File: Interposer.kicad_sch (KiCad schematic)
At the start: 22 parts, among them J19 Conn_01x04_Pin, U13 TCA9548APWR, U14 ESP32-DEVKIT-V1

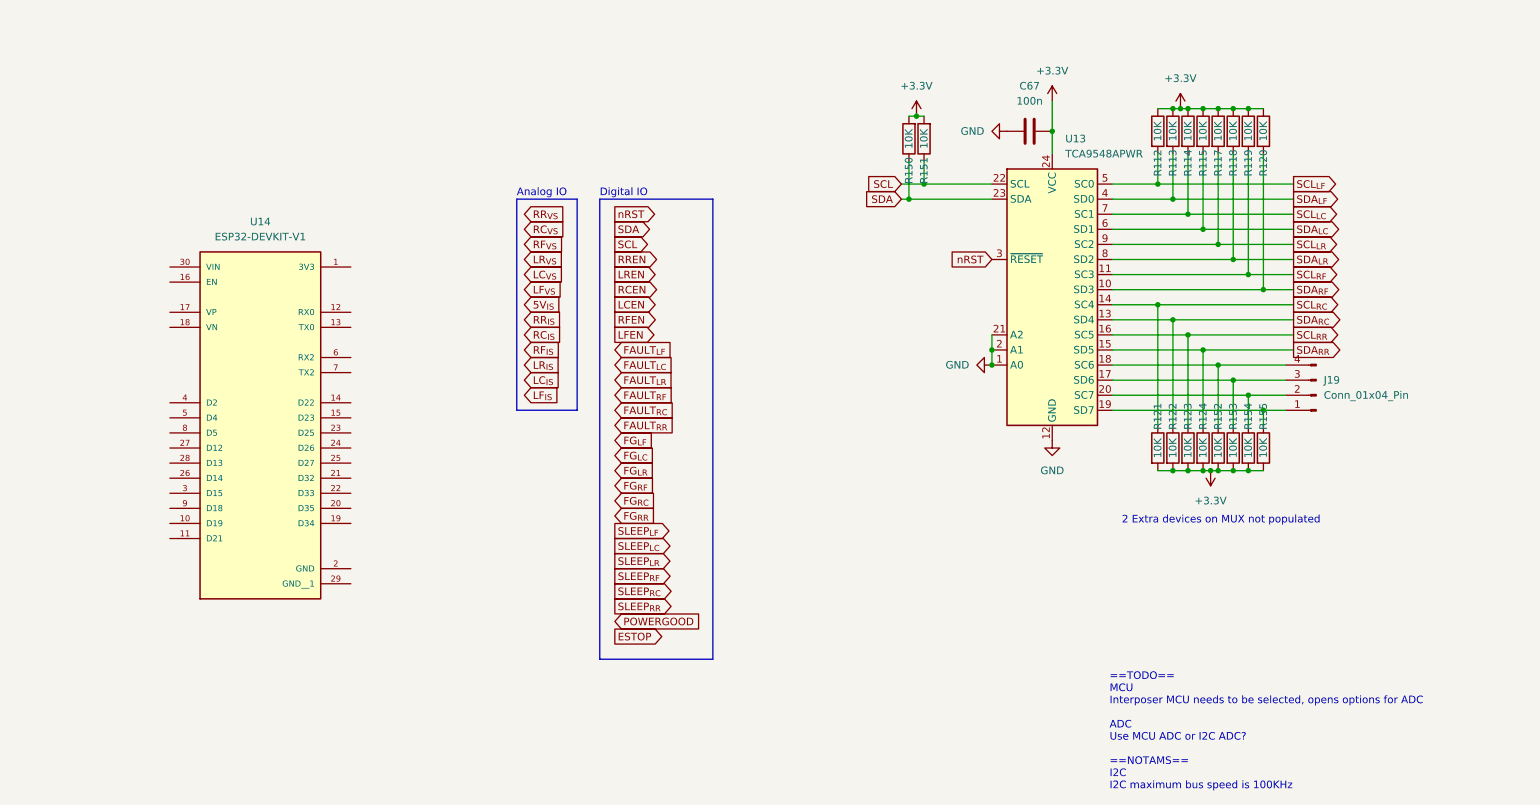
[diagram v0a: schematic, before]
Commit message: The great decluttering
Moved all possible controls to I2C, part selection commenced, IOs assigned pending comms schema
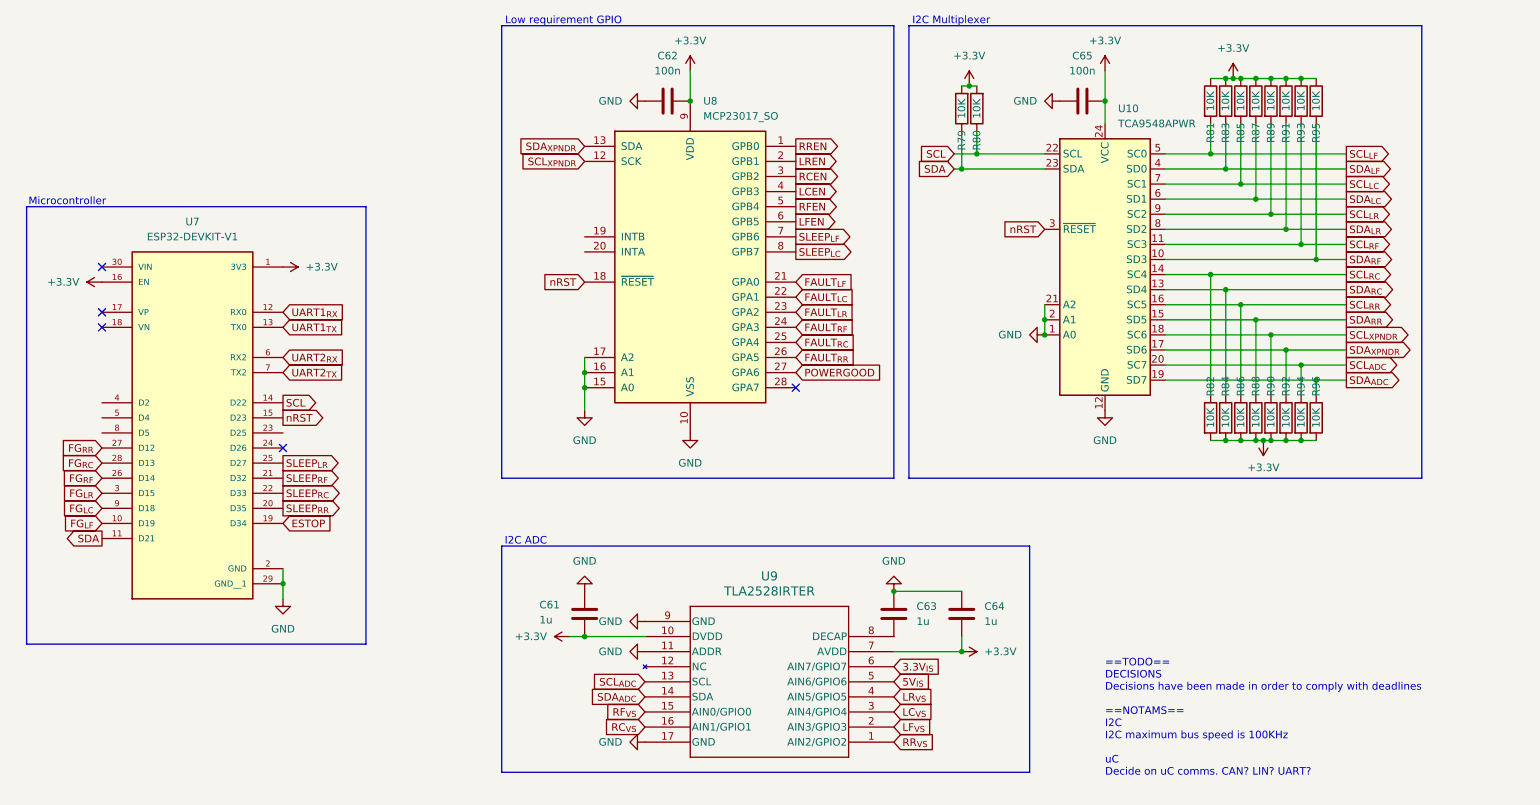
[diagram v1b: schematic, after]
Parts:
- removed J19: Conn_01x04_Pin, symbol Connector:Conn_01x04_Pin
- added C61, C63, C64: 1u, Capacitor_SMD:C_0603_1608Metric, symbol Device:C
- added C62: 100n, Capacitor_SMD:C_0603_1608Metric, symbol Device:C
- added U8: MCP23017_SO, Package_SO:SOIC-28W_7.5x17.9mm_P1.27mm, symbol Interface_Expansion:MCP23017_SO
- added U9: TLA2528IRTER, WQFN16_RTE_TEX, symbol TLA2528IRTER:TLA2528IRTER
- renumbered C67 to C65, R150 to R79, R151 to R80, R112 to R81, R121 to R82, R113 to R83, R122 to R84, R114 to R85, R123 to R86, R115 to R87, R124 to R88, R117 to R89, R152 to R90, R118 to R91, R153 to R92, R119 to R93, R154 to R94, R120 to R95, R155 to R96, U13 to U10, U14 to U7
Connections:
- net +3.3V: now also U7.1 (3V3), U7.16 (EN), C61.1, C62.2, C64.2, U8.9 (VDD), U9.10 (DVDD), U9.7 (AVDD)
- net 5V_{IS}: now also U9.5 (AIN6/GPIO6)
- net ESTOP: now also U7.19 (D34)
- net FAULT_{LC}: now also U8.22 (GPA1)
- net FAULT_{LF}: now also U8.21 (GPA0)
- net FAULT_{LR}: now also U8.23 (GPA2)
- net FAULT_{RC}: now also U8.25 (GPA4)
- net FAULT_{RF}: now also U8.24 (GPA3)
- net FAULT_{RR}: now also U8.26 (GPA5)
- net FG_{LC}: now also U7.9 (D18)
- net FG_{LF}: now also U7.10 (D19)
- net FG_{LR}: now also U7.3 (D15)
- net FG_{RC}: now also U7.28 (D13)
- net FG_{RF}: now also U7.26 (D14)
- net FG_{RR}: now also U7.27 (D12)
- net GND: now also U7.2 (GND), U7.29 (GND__1), C61.2, C62.1, C63.1, C64.1, U8.10 (VSS), U8.15 (A0), U8.16 (A1), U8.17 (A2), U9.11 (ADDR), U9.17 (GND), U9.9 (GND)
- net LCEN: now also U8.4 (GPB3)
- net LC_{VS}: now also U9.3 (AIN4/GPIO4)
- net LFEN: now also U8.6 (GPB5)
- net LF_{VS}: now also U9.2 (AIN3/GPIO3)
- net LREN: now also U8.2 (GPB1)
- net LR_{VS}: now also U9.4 (AIN5/GPIO5)
- net POWERGOOD: now also U8.27 (GPA6)
- net RCEN: now also U8.3 (GPB2)
- net RC_{VS}: now also U9.16 (AIN1/GPIO1)
- net RFEN: now also U8.5 (GPB4)
- net RF_{VS}: now also U9.15 (AIN0/GPIO0)
- net RREN: now also U8.1 (GPB0)
- net RR_{VS}: now also U9.1 (AIN2/GPIO2)
- net SCL: now also U7.14 (D22)
- net SDA: now also U7.11 (D21)
- net SLEEP_{LC}: now also U8.8 (GPB7)
- net SLEEP_{LF}: now also U8.7 (GPB6)
- net SLEEP_{LR}: now also U7.25 (D27)
- net SLEEP_{RC}: now also U7.22 (D33)
- net SLEEP_{RF}: now also U7.21 (D32)
- net SLEEP_{RR}: now also U7.20 (D35)
- net nRST: now also U7.15 (D23), U8.18 (~{RESET})
- net SCL_{ADC}: now reaches R94.1, U10.20 (SC7)
- net SCL_{ADC}: now also U9.13 (SCL)
- net SDA_{XPNDR}: now reaches R92.1, U10.17 (SD6)
- net SDA_{XPNDR}: now also U8.13 (SDA)
- net SCL_{XPNDR}: now reaches R90.1, U10.18 (SC6)
- net SCL_{XPNDR}: now also U8.12 (SCK)
- net SDA_{ADC}: now reaches R96.1, U10.19 (SD7)
- net SDA_{ADC}: now also U9.14 (SDA)
- net UART1_{RX}: now reaches U7.12 (RX0)
- net UART1_{TX}: now reaches U7.13 (TX0)
- net UART2_{RX}: now reaches U7.6 (RX2)
- net UART2_{TX}: now reaches U7.7 (TX2)
- new net: C63.2, U9.8 (DECAP)
- new net 3.3V_{IS}: U9.6 (AIN7/GPIO7)
- no-connect marks 0 -> 5
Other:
- note added: "==TODO== DECISIONS Decisions have been made in order to comply with deadlines ==NOTAMS== I2C I2C maximum bus speed is 100KHz uC Decide on uC comms. CAN? LIN? UART?"
- note added: "I2C ADC"
- note added: "I2C Multiplexer"
- note added: "Low requirement GPIO"
- note added: "Microcontroller"
- note removed: "2 Extra devices on MUX not populated"
- note removed: "==TODO== MCU Interposer MCU needs to be selected, opens options for ADC ADC Use MCU ADC or I2C ADC? ==NOTAMS== I2C I2C maximum bus speed is 100KHz"
- note removed: "Analog IO"
- note removed: "Digital IO"
- moved on the sheet: C65, R79, R80, R81, R82, R83, R84, R85, R86, R87, R88, R89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

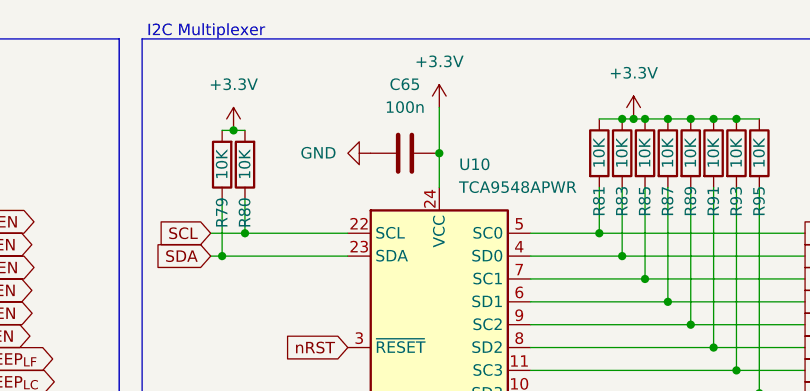
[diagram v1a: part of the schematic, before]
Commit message: Powerstage
Powerstage layout, non critical changes to schematic
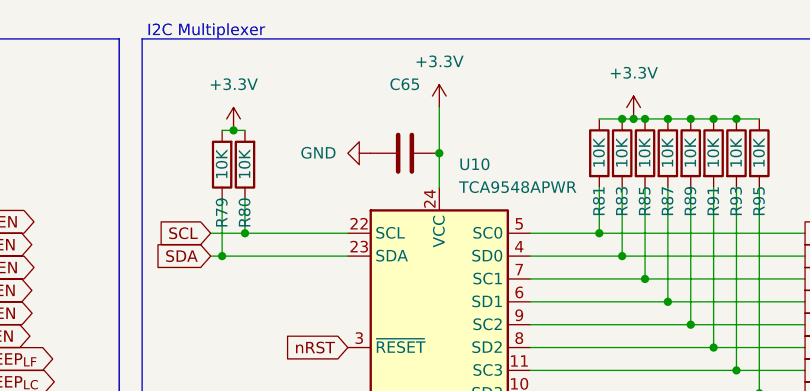
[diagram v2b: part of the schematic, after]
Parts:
- C61, C62, C63, C64: footprint Capacitor_SMD:C_0603_1608Metric -> Capacitor_SMD:C_0201_0603Metric
- C65: value 100n -> ~; footprint Capacitor_SMD:C_0603_1608Metric -> Capacitor_SMD:C_0201_0603Metric
- R79, R80, R81, R82, R83, R84, R85, R86, R87, R88, R89, R90, R91, R92, R93, R94, R95, R96: footprint Resistor_SMD:R_0603_1608Metric_Pad0.98x0.95mm_HandSolder -> Resistor_SMD:R_0201_0603Metric
